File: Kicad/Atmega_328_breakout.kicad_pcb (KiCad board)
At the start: 2 copper layers, 73.8 x 62 mm, 71 parts, among them J1 Jack-DC, J10 Conn_01x06, J11 01x03, J12 01x03, J13 01x03, J14 01x03, J15 01x03, J16 01x03, J17 01x03, J18 01x03, J19 Power_connector, J2 01x03, J20 ADC_Connector, J21 PORB++_connector, J22 PORD_connector, J23 Conn_01x01, J24 Device_Connector, J25 Pin out, J26 Com_header, J27 Power terminal, J28 USB, J3 01x03, J4 01x03, J5 01x03, J6 01x03, J7 01x03, J8 01x03, J9 01x03, Q1 AO3401A, SW1 SW_Push, SW2 SW_Push, U1 NCP1117-5, U2 L7805, U3 LM358, U4 ATMEGA328P-AU, U5 MCP1700-33, U6 MCP2221, Y1 Crystal_GND24

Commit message: Initial push
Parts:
- removed SHIELD1: ATMEL_SHIELD, jorgen:AtmelSHIELD
- added C15: 100n, Capacitor_SMD:C_0402_1005Metric, F.Cu at (63.6, 75.7)
- added C16: 100n, Capacitor_SMD:C_0402_1005Metric, F.Cu at (60.0, 76.7)
- added R10: 120, Resistor_SMD:R_0402_1005Metric, F.Cu at (62.4, 75.7)
- added R13: 120, Resistor_SMD:R_0402_1005Metric, F.Cu at (61.2, 75.7)
- U6: value MCP2221 -> CH340E; footprint Package_SO:TSSOP-14_4.4x5mm_P0.65mm -> Package_SO:MSOP-10_3x3mm_P0.5mm
- moved U6 3.58 mm to (62.0, 80.1), turned to 90 degrees
- moved C14 2.33 mm to (57.8, 77.7)
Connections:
- U6 pad 1: VCC -> Net-(J28-Pad3)
- U6 pad 2: Net-(U6-Pad2) -> Net-(J28-Pad2)
- U6 pad 3: Net-(U6-Pad3) -> GND
- U6 pad 5: PD1(TX) -> Net-(U6-Pad5)
- U6 pad 6: PD0(RX) -> Net-(U6-Pad6)
- U6 pad 7: Net-(U6-Pad7) -> VCC
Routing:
- net ~RESET: track 108.9 -> 91.5 mm, vias 4 -> 3
- net PD1(TX): track 77.1 -> 64.0 mm
- net VCC: track 209.4 -> 196.3 mm
- net VUSB: track 16.2 -> 3.88 mm
- net GND: track 77.6 -> 65.6 mm, vias 14 -> 15
- net PD0(RX): track 78.0 -> 66.5 mm
- net Net-(R10-Pad1): track 0.00 -> 1.86 mm
- net Net-(R13-Pad1): track 0.00 -> 1.81 mm
- net Net-(C16-Pad2): track 0.00 -> 1.30 mm
- net Net-(J28-Pad3): track 7.47 -> 6.45 mm
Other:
- board text removed: "MCP2221"

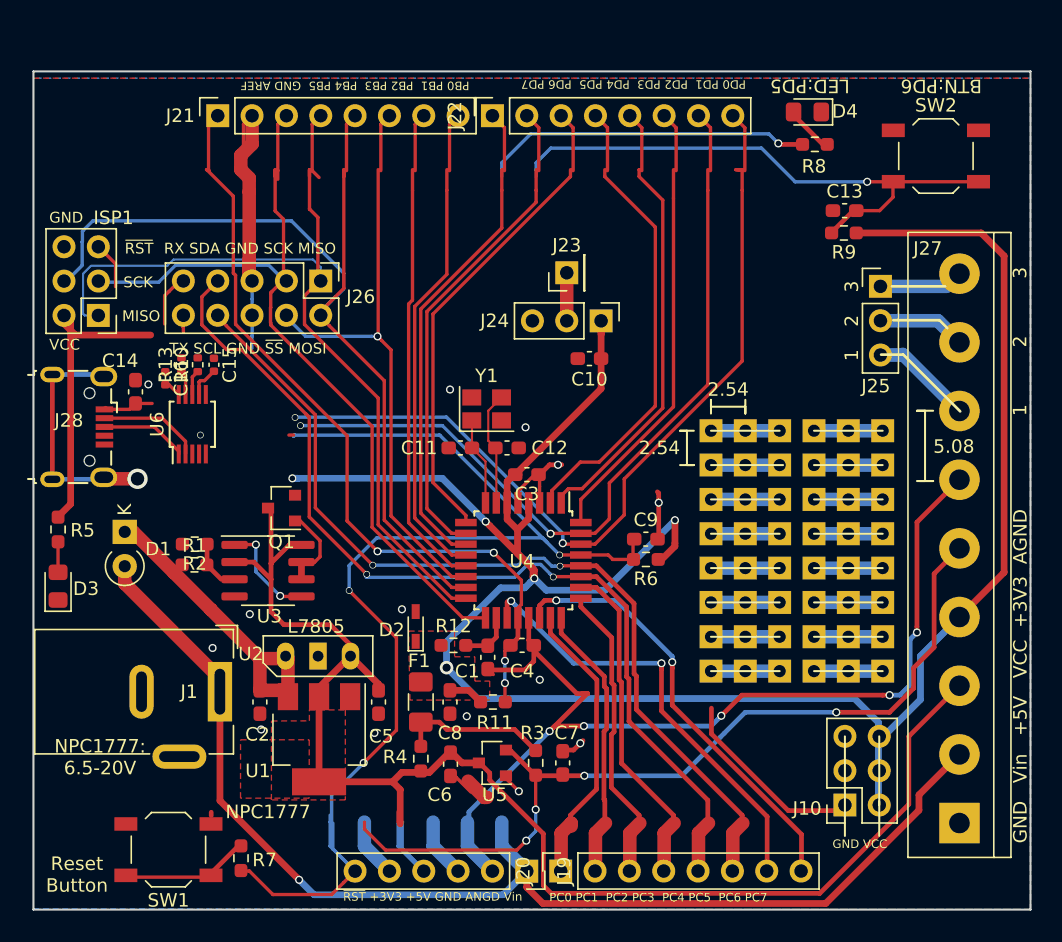
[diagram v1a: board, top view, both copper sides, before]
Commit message: replaced serial to usb chip and added safety.
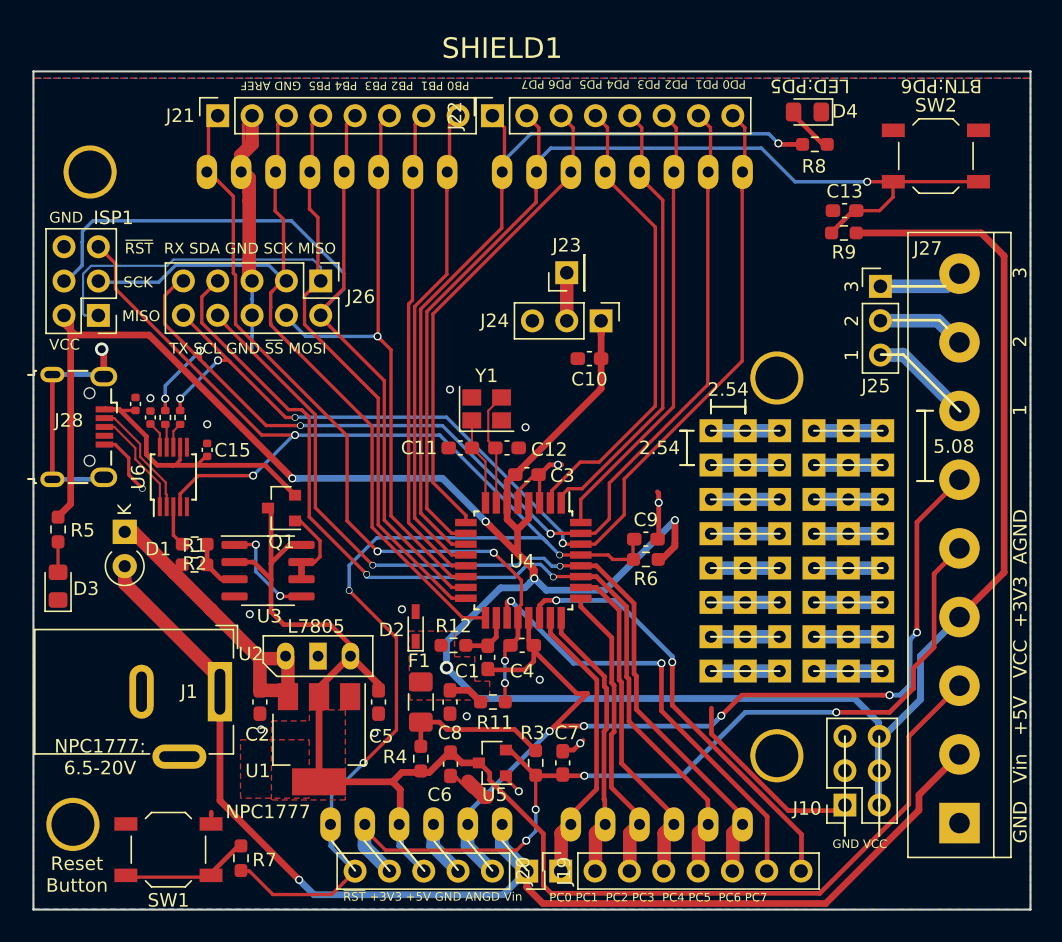
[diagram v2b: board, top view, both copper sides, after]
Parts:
- added SHIELD1: ATMEL_SHIELD, jorgen:AtmelSHIELD, F.Cu at (50.4, 115.8)
- C14: footprint Capacitor_SMD:C_0603_1608Metric_Pad1.08x0.95mm_HandSolder -> Capacitor_SMD:C_0402_1005Metric
- R10, R13: value 120 -> 200
- moved C15 6.32 mm to (63.1, 82.0)
- moved U6 4.14 mm to (60.6, 84.0)
- moved R10 4.11 mm to (61.1, 79.6)
- moved R13 4.08 mm to (60.0, 79.6)
- moved C16 3.10 mm to (58.9, 79.6)
- moved C14 0.90 mm to (57.8, 78.6)
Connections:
- C15 pad 2: VCC -> VUSB
- U6 pad 7: VCC -> VUSB
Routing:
- net ~RESET: track 91.5 -> 120.5 mm, vias 3 -> 5
- net PD1(TX): track 64.0 -> 83.3 mm, vias 2 -> 4
- net VUSB: track 3.88 -> 21.9 mm
- net PD0(RX): track 66.5 -> 81.9 mm, vias 2 -> 4
- net VCC: track 196.3 -> 208.8 mm
- net GND: track 65.6 -> 74.3 mm
- net Net-(J28-Pad3): track 6.45 -> 8.23 mm
- net Net-(J28-Pad2): track 7.65 -> 9.00 mm
- net Net-(C16-Pad2): track 1.30 -> 2.01 mm
